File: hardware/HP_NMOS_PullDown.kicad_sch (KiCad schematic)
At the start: 4 parts, among them Q5 STN4NF06L

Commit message: relay new driving logic, some ltc communication changes
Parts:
- D12: value 4A/80V -> VSSB410S-E3/52T
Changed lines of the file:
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@@
 			)
 		)
-		(property "Value" "4A/80V"
+		(property "Value" "VSSB410S-E3/52T"
 			(at 146.685 76.1999 90)
 			(effects

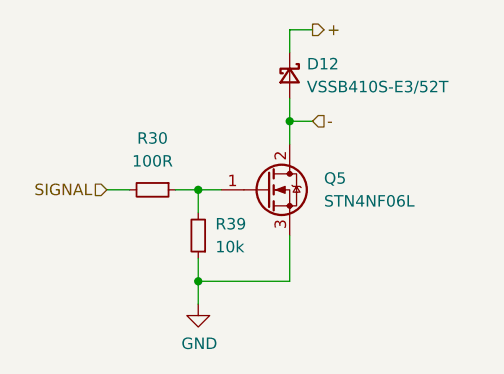
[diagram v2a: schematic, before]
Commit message: relay new driving logic, some ltc communication changes
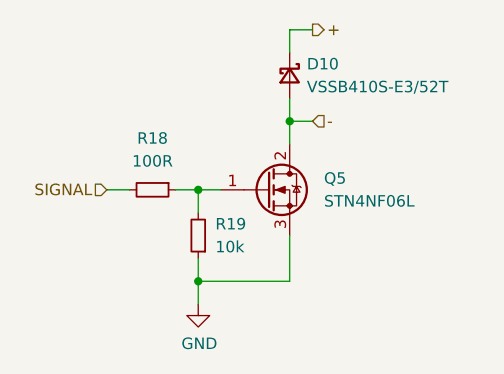
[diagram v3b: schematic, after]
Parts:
- renumbered D12 to D10, R30 to R18, R39 to R19
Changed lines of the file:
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@@
 		(dnp no)
 		(fields_autoplaced yes)
-		(property "Reference" "R39"
+		(property "Reference" "R19"
 			(at 136.525 91.4399 0)
 			(effects
@@
 			(project "PUTM_EV_BMS_HV_Master_2021"
 				(path "/b456cffc-d9d7-4c91-91f2-36ec9a65dd1b/6eb4a2b1-8e5b-451b-b593-8aaaa3a4213e/649ea10f-ddf7-49be-afe9-7c2c999df872"
-					(reference "R39")
+					(reference "R19")
 					(unit 1)
 				)
 				(path "/b456cffc-d9d7-4c91-91f2-36ec9a65dd1b/6eb4a2b1-8e5b-451b-b593-8aaaa3a4213e/67d08ddd-b8e9-4f40-a055-93108463bf84"
-					(reference "R28")
+					(reference "R17")
 					(unit 1)
 				)
 				(path "/b456cffc-d9d7-4c91-91f2-36ec9a65dd1b/6eb4a2b1-8e5b-451b-b593-8aaaa3a4213e/fd8c1b79-afed-4653-bb63-44888bf7ecb3"
-					(reference "R46")
+					(reference "R67")
 					(unit 1)
 				)
@@
 		(dnp no)
 		(fields_autoplaced yes)
-		(property "Reference" "R30"
+		(property "Reference" "R18"
 			(at 129.54 81.915 90)
 			(effects
@@
 			(project "PUTM_EV_BMS_HV_Master_2021"
 				(path "/b456cffc-d9d7-4c91-91f2-36ec9a65dd1b/6eb4a2b1-8e5b-451b-b593-8aaaa3a4213e/649ea10f-ddf7-49be-afe9-7c2c999df872"
-					(reference "R30")
+					(reference "R18")
 					(unit 1)
 				)
 				(path "/b456cffc-d9d7-4c91-91f2-36ec9a65dd1b/6eb4a2b1-8e5b-451b-b593-8aaaa3a4213e/67d08ddd-b8e9-4f40-a055-93108463bf84"
-					(reference "R22")
+					(reference "R16")
 					(unit 1)
 				)
 				(path "/b456cffc-d9d7-4c91-91f2-36ec9a65dd1b/6eb4a2b1-8e5b-451b-b593-8aaaa3a4213e/fd8c1b79-afed-4653-bb63-44888bf7ecb3"
-					(reference "R43")
+					(reference "R66")
 					(unit 1)
 				)
@@
 				)
 				(path "/b456cffc-d9d7-4c91-91f2-36ec9a65dd1b/6eb4a2b1-8e5b-451b-b593-8aaaa3a4213e/67d08ddd-b8e9-4f40-a055-93108463bf84"
-					(reference "Q3")
+					(reference "Q4")
 					(unit 1)
 				)
 				(path "/b456cffc-d9d7-4c91-91f2-36ec9a65dd1b/6eb4a2b1-8e5b-451b-b593-8aaaa3a4213e/fd8c1b79-afed-4653-bb63-44888bf7ecb3"
-					(reference "Q6")
+					(reference "Q13")
 					(unit 1)
 				)
@@
 		(dnp no)
 		(fields_autoplaced yes)
-		(property "Reference" "D12"
+		(property "Reference" "D10"
 			(at 146.685 73.6599 90)
 			(effects
@@
 			(project "PUTM_EV_BMS_HV_Master_2021"
 				(path "/b456cffc-d9d7-4c91-91f2-36ec9a65dd1b/6eb4a2b1-8e5b-451b-b593-8aaaa3a4213e/649ea10f-ddf7-49be-afe9-7c2c999df872"
-					(reference "D12")
+					(reference "D10")
 					(unit 1)
 				)
 				(path "/b456cffc-d9d7-4c91-91f2-36ec9a65dd1b/6eb4a2b1-8e5b-451b-b593-8aaaa3a4213e/67d08ddd-b8e9-4f40-a055-93108463bf84"
-					(reference "D4")
+					(reference "D9")
 					(unit 1)
 				)
 				(path "/b456cffc-d9d7-4c91-91f2-36ec9a65dd1b/6eb4a2b1-8e5b-451b-b593-8aaaa3a4213e/fd8c1b79-afed-4653-bb63-44888bf7ecb3"
-					(reference "D13")
+					(reference "D24")
 					(unit 1)
 				)
@@
 		(on_board yes)
 		(dnp no)
-		(property "Reference" "#PWR0126"
+		(property "Reference" "#PWR054"
 			(at 134.62 106.68 0)
 			(effects
@@
 			(project "PUTM_EV_BMS_HV_Master_2021"
 				(path "/b456cffc-d9d7-4c91-91f2-36ec9a65dd1b/6eb4a2b1-8e5b-451b-b593-8aaaa3a4213e/649ea10f-ddf7-49be-afe9-7c2c999df872"
-					(reference "#PWR0126")
+					(reference "#PWR054")
 					(unit 1)
 				)
 				(path "/b456cffc-d9d7-4c91-91f2-36ec9a65dd1b/6eb4a2b1-8e5b-451b-b593-8aaaa3a4213e/67d08ddd-b8e9-4f40-a055-93108463bf84"
-					(reference "#PWR0120")
+					(reference "#PWR053")
 					(unit 1)
 				)
 				(path "/b456cffc-d9d7-4c91-91f2-36ec9a65dd1b/6eb4a2b1-8e5b-451b-b593-8aaaa3a4213e/fd8c1b79-afed-4653-bb63-44888bf7ecb3"
-					(reference "#PWR0127")
-					(unit 1)
-				)
+					(reference "#PWR0119")
+					(unit 1)
+				)

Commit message: major schematic changes
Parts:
- renumbered D10 to D9, Q5 to Q4, R18 to R16, R19 to R17
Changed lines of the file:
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@@
 		(dnp no)
 		(fields_autoplaced yes)
-		(property "Reference" "R19"
+		(property "Reference" "R17"
 			(at 136.525 91.4399 0)
 			(effects
@@
 		(instances
 			(project "PUTM_EV_BMS_HV_MASTER_2023"
-				(path "/b456cffc-d9d7-4c91-91f2-36ec9a65dd1b/6eb4a2b1-8e5b-451b-b593-8aaaa3a4213e/649ea10f-ddf7-49be-afe9-7c2c999df872"
+				(path "/b456cffc-d9d7-4c91-91f2-36ec9a65dd1b/29791d59-2030-4558-a08d-30d921be5366"
 					(reference "R19")
 					(unit 1)
 				)
-				(path "/b456cffc-d9d7-4c91-91f2-36ec9a65dd1b/6eb4a2b1-8e5b-451b-b593-8aaaa3a4213e/67d08ddd-b8e9-4f40-a055-93108463bf84"
+				(path "/b456cffc-d9d7-4c91-91f2-36ec9a65dd1b/b4a6be2b-8020-42af-b7ee-28b8df6b160d"
+					(reference "R67")
+					(unit 1)
+				)
+				(path "/b456cffc-d9d7-4c91-91f2-36ec9a65dd1b/cf816e51-40ee-487b-9eb2-6f04c3c93be5"
 					(reference "R17")
-					(unit 1)
-				)
-				(path "/b456cffc-d9d7-4c91-91f2-36ec9a65dd1b/6eb4a2b1-8e5b-451b-b593-8aaaa3a4213e/fd8c1b79-afed-4653-bb63-44888bf7ecb3"
-					(reference "R67")
 					(unit 1)
 				)
@@
 		(dnp no)
 		(fields_autoplaced yes)
-		(property "Reference" "R18"
+		(property "Reference" "R16"
 			(at 129.54 81.915 90)
 			(effects
@@
 		(instances
 			(project "PUTM_EV_BMS_HV_MASTER_2023"
-				(path "/b456cffc-d9d7-4c91-91f2-36ec9a65dd1b/6eb4a2b1-8e5b-451b-b593-8aaaa3a4213e/649ea10f-ddf7-49be-afe9-7c2c999df872"
+				(path "/b456cffc-d9d7-4c91-91f2-36ec9a65dd1b/29791d59-2030-4558-a08d-30d921be5366"
 					(reference "R18")
 					(unit 1)
 				)
-				(path "/b456cffc-d9d7-4c91-91f2-36ec9a65dd1b/6eb4a2b1-8e5b-451b-b593-8aaaa3a4213e/67d08ddd-b8e9-4f40-a055-93108463bf84"
+				(path "/b456cffc-d9d7-4c91-91f2-36ec9a65dd1b/b4a6be2b-8020-42af-b7ee-28b8df6b160d"
+					(reference "R66")
+					(unit 1)
+				)
+				(path "/b456cffc-d9d7-4c91-91f2-36ec9a65dd1b/cf816e51-40ee-487b-9eb2-6f04c3c93be5"
 					(reference "R16")
-					(unit 1)
-				)
-				(path "/b456cffc-d9d7-4c91-91f2-36ec9a65dd1b/6eb4a2b1-8e5b-451b-b593-8aaaa3a4213e/fd8c1b79-afed-4653-bb63-44888bf7ecb3"
-					(reference "R66")
 					(unit 1)
 				)
@@
 		(dnp no)
 		(fields_autoplaced yes)
-		(property "Reference" "Q5"
+		(property "Reference" "Q4"
 			(at 148.59 86.36 0)
 			(effects
@@
 		(instances
 			(project "PUTM_EV_BMS_HV_MASTER_2023"
-				(path "/b456cffc-d9d7-4c91-91f2-36ec9a65dd1b/6eb4a2b1-8e5b-451b-b593-8aaaa3a4213e/649ea10f-ddf7-49be-afe9-7c2c999df872"
+				(path "/b456cffc-d9d7-4c91-91f2-36ec9a65dd1b/29791d59-2030-4558-a08d-30d921be5366"
 					(reference "Q5")
 					(unit 1)
 				)
-				(path "/b456cffc-d9d7-4c91-91f2-36ec9a65dd1b/6eb4a2b1-8e5b-451b-b593-8aaaa3a4213e/67d08ddd-b8e9-4f40-a055-93108463bf84"
+				(path "/b456cffc-d9d7-4c91-91f2-36ec9a65dd1b/b4a6be2b-8020-42af-b7ee-28b8df6b160d"
+					(reference "Q13")
+					(unit 1)
+				)
+				(path "/b456cffc-d9d7-4c91-91f2-36ec9a65dd1b/cf816e51-40ee-487b-9eb2-6f04c3c93be5"
 					(reference "Q4")
-					(unit 1)
-				)
-				(path "/b456cffc-d9d7-4c91-91f2-36ec9a65dd1b/6eb4a2b1-8e5b-451b-b593-8aaaa3a4213e/fd8c1b79-afed-4653-bb63-44888bf7ecb3"
-					(reference "Q13")
 					(unit 1)
 				)
@@
 		(dnp no)
 		(fields_autoplaced yes)
-		(property "Reference" "D10"
+		(property "Reference" "D9"
 			(at 146.685 73.6599 90)
 			(effects
@@
 		(instances
 			(project "PUTM_EV_BMS_HV_MASTER_2023"
-				(path "/b456cffc-d9d7-4c91-91f2-36ec9a65dd1b/6eb4a2b1-8e5b-451b-b593-8aaaa3a4213e/649ea10f-ddf7-49be-afe9-7c2c999df872"
+				(path "/b456cffc-d9d7-4c91-91f2-36ec9a65dd1b/29791d59-2030-4558-a08d-30d921be5366"
 					(reference "D10")
 					(unit 1)
 				)
-				(path "/b456cffc-d9d7-4c91-91f2-36ec9a65dd1b/6eb4a2b1-8e5b-451b-b593-8aaaa3a4213e/67d08ddd-b8e9-4f40-a055-93108463bf84"
+				(path "/b456cffc-d9d7-4c91-91f2-36ec9a65dd1b/b4a6be2b-8020-42af-b7ee-28b8df6b160d"
+					(reference "D24")
+					(unit 1)
+				)
+				(path "/b456cffc-d9d7-4c91-91f2-36ec9a65dd1b/cf816e51-40ee-487b-9eb2-6f04c3c93be5"
 					(reference "D9")
-					(unit 1)
-				)
-				(path "/b456cffc-d9d7-4c91-91f2-36ec9a65dd1b/6eb4a2b1-8e5b-451b-b593-8aaaa3a4213e/fd8c1b79-afed-4653-bb63-44888bf7ecb3"
-					(reference "D24")
 					(unit 1)
 				)
@@
 		(on_board yes)
 		(dnp no)
-		(property "Reference" "#PWR054"
+		(property "Reference" "#PWR053"
 			(at 134.62 106.68 0)
 			(effects
@@
 		(instances
 			(project "PUTM_EV_BMS_HV_MASTER_2023"
-				(path "/b456cffc-d9d7-4c91-91f2-36ec9a65dd1b/6eb4a2b1-8e5b-451b-b593-8aaaa3a4213e/649ea10f-ddf7-49be-afe9-7c2c999df872"
+				(path "/b456cffc-d9d7-4c91-91f2-36ec9a65dd1b/29791d59-2030-4558-a08d-30d921be5366"
 					(reference "#PWR054")
 					(unit 1)
 				)
-				(path "/b456cffc-d9d7-4c91-91f2-36ec9a65dd1b/6eb4a2b1-8e5b-451b-b593-8aaaa3a4213e/67d08ddd-b8e9-4f40-a055-93108463bf84"
+				(path "/b456cffc-d9d7-4c91-91f2-36ec9a65dd1b/b4a6be2b-8020-42af-b7ee-28b8df6b160d"
+					(reference "#PWR081")
+					(unit 1)
+				)
+				(path "/b456cffc-d9d7-4c91-91f2-36ec9a65dd1b/cf816e51-40ee-487b-9eb2-6f04c3c93be5"
 					(reference "#PWR053")
 					(unit 1)
 				)
-				(path "/b456cffc-d9d7-4c91-91f2-36ec9a65dd1b/6eb4a2b1-8e5b-451b-b593-8aaaa3a4213e/fd8c1b79-afed-4653-bb63-44888bf7ecb3"
-					(reference "#PWR0119")
-					(unit 1)
-				)
